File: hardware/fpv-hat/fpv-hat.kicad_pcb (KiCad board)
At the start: 2 copper layers, 100 x 65 mm, 0 parts

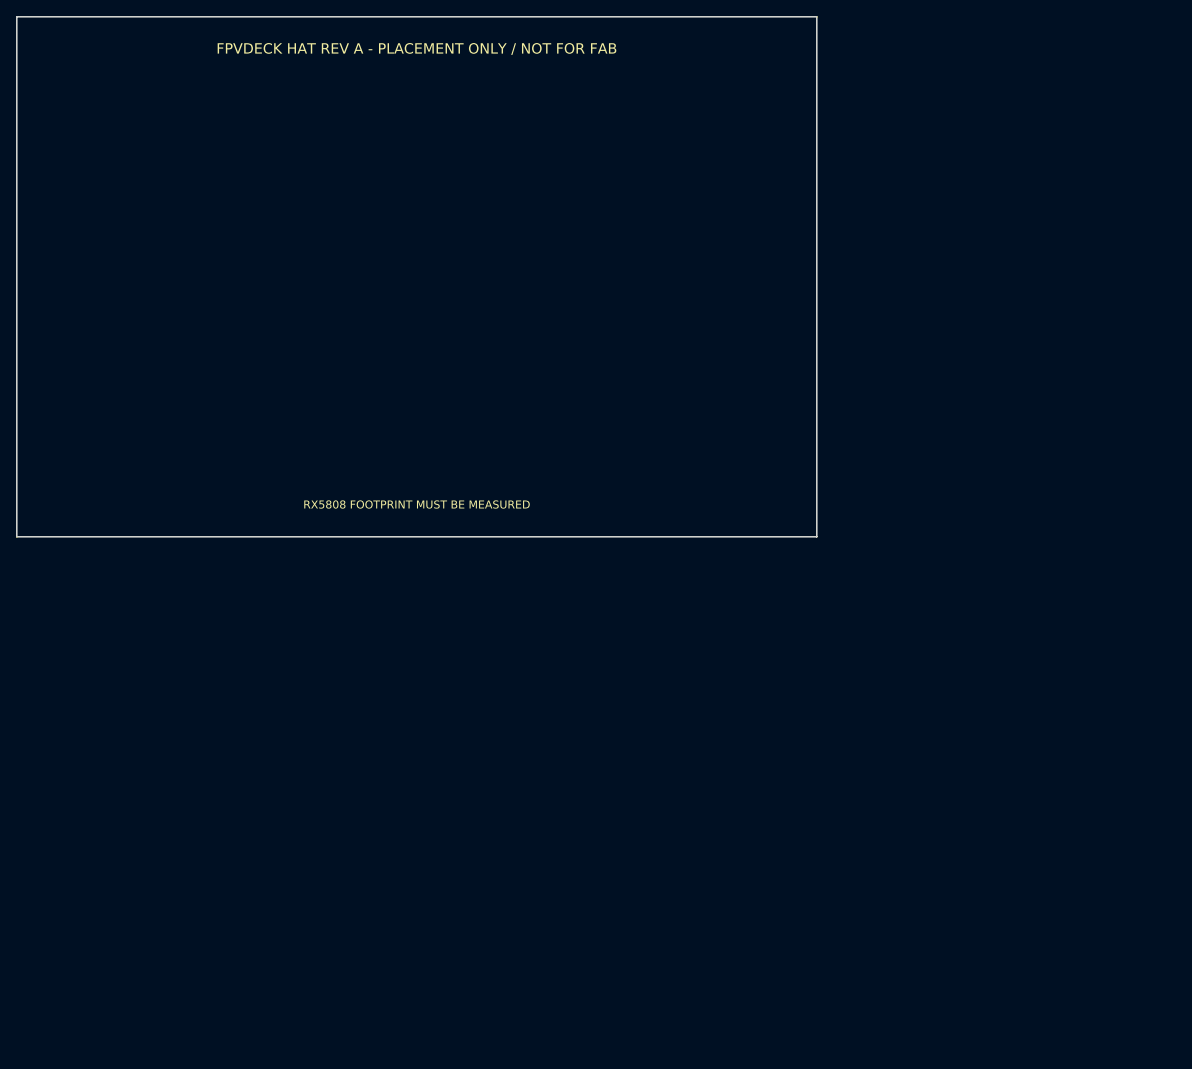
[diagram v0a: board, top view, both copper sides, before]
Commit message: feat(cad): add prototype enclosure and HAT placement model
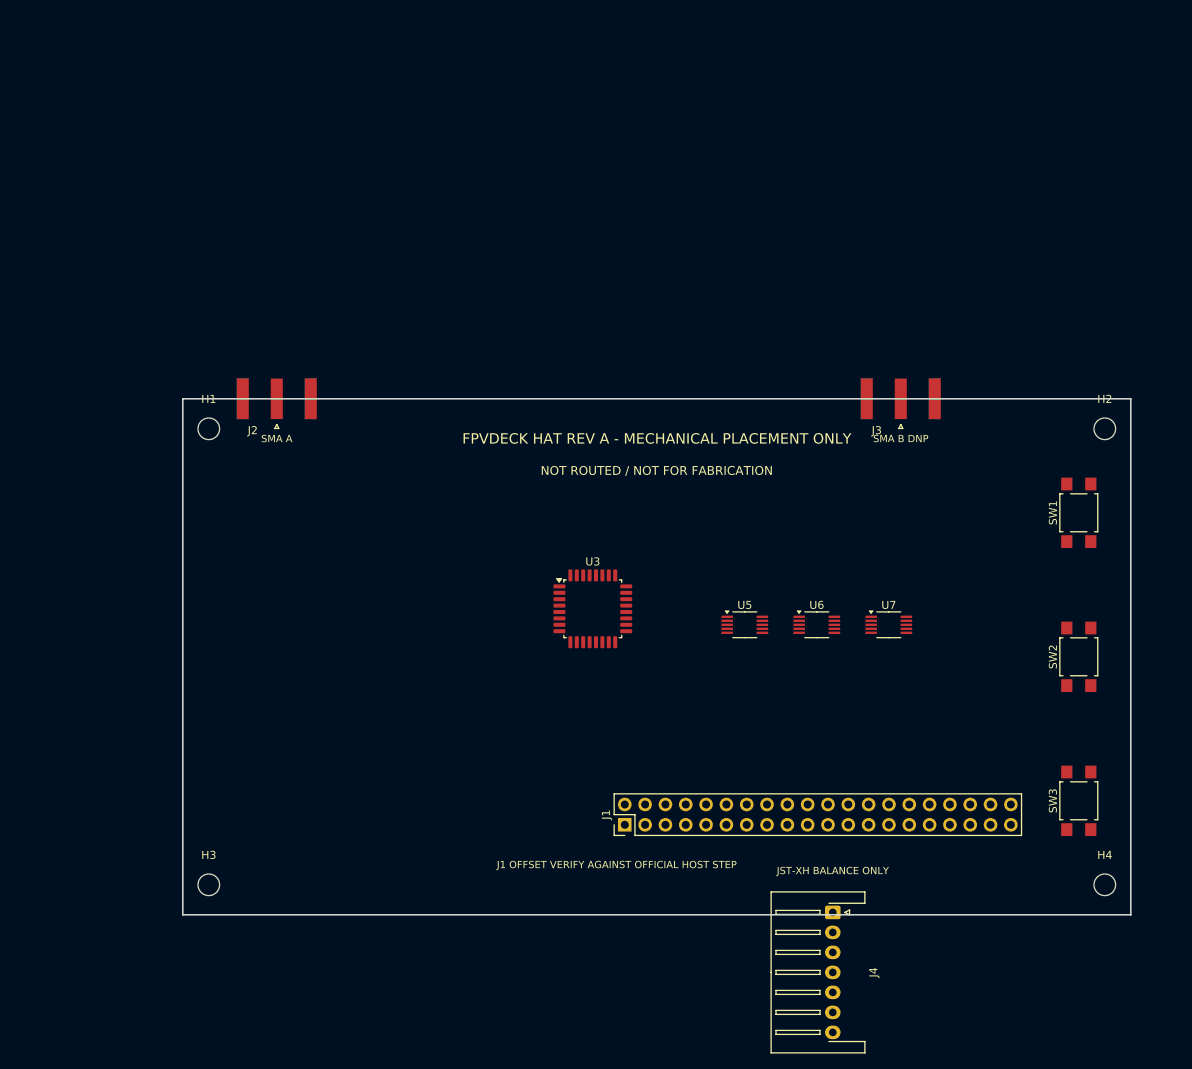
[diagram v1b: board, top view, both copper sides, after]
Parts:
- added H1: MountingHole_2.7mm_M2.5, MountingHole_2.7mm_M2.5, F.Cu at (44.0, 71.5)
- added H2: MountingHole_2.7mm_M2.5, MountingHole_2.7mm_M2.5, F.Cu at (156.0, 71.5)
- added H3: MountingHole_2.7mm_M2.5, MountingHole_2.7mm_M2.5, F.Cu at (44.0, 128.5)
- added H4: MountingHole_2.7mm_M2.5, MountingHole_2.7mm_M2.5, F.Cu at (156.0, 128.5)
- added J1: PinHeader_2x20_P2.54mm_Vertical, PinHeader_2x20_P2.54mm_Vertical, F.Cu at (96.0, 121.0)
- added J2: SMA_Amphenol_132289_EdgeMount, SMA_Amphenol_132289_EdgeMount, F.Cu at (52.5, 67.8)
- added J3: SMA_Amphenol_132289_EdgeMount, SMA_Amphenol_132289_EdgeMount, F.Cu at (130.5, 67.8)
- added J4: JST_XH_S7B-XH-A-1_1x07_P2.50mm_Horizontal, JST_XH_S7B-XH-A-1_1x07_P2.50mm_Horizontal, F.Cu at (122.0, 131.9)
- added SW1: SW_SPST_TL3305A, SW_SPST_TL3305A, F.Cu at (152.8, 82.0)
- added SW2: SW_SPST_TL3305A, SW_SPST_TL3305A, F.Cu at (152.8, 100.0)
- added SW3: SW_SPST_TL3305A, SW_SPST_TL3305A, F.Cu at (152.8, 118.0)
- added U3: LQFP-32_7x7mm_P0.8mm, LQFP-32_7x7mm_P0.8mm, F.Cu at (92.0, 94.0)
- added U5: VSSOP-10_3x3mm_P0.5mm, VSSOP-10_3x3mm_P0.5mm, F.Cu at (111.0, 96.0)
- added U6: VSSOP-10_3x3mm_P0.5mm, VSSOP-10_3x3mm_P0.5mm, F.Cu at (120.0, 96.0)
- added U7: VSSOP-10_3x3mm_P0.5mm, VSSOP-10_3x3mm_P0.5mm, F.Cu at (129.0, 96.0)
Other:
- board size 100 x 65 mm -> 118.5 x 64.5 mm
- board text added: "FPVDECK HAT REV A - MECHANICAL PLACEMENT ONLY"
- board text added: "J1 OFFSET VERIFY AGAINST OFFICIAL HOST STEP"
- board text added: "JST-XH BALANCE ONLY"
- board text added: "NOT ROUTED / NOT FOR FABRICATION"
- board text added: "SMA A"
- board text added: "SMA B DNP"
- board text removed: "FPVDECK HAT REV A - PLACEMENT ONLY / NOT FOR FAB"
- board text removed: "RX5808 FOOTPRINT MUST BE MEASURED"

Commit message: feat(hw): add dual RX5808 final-form HAT layout
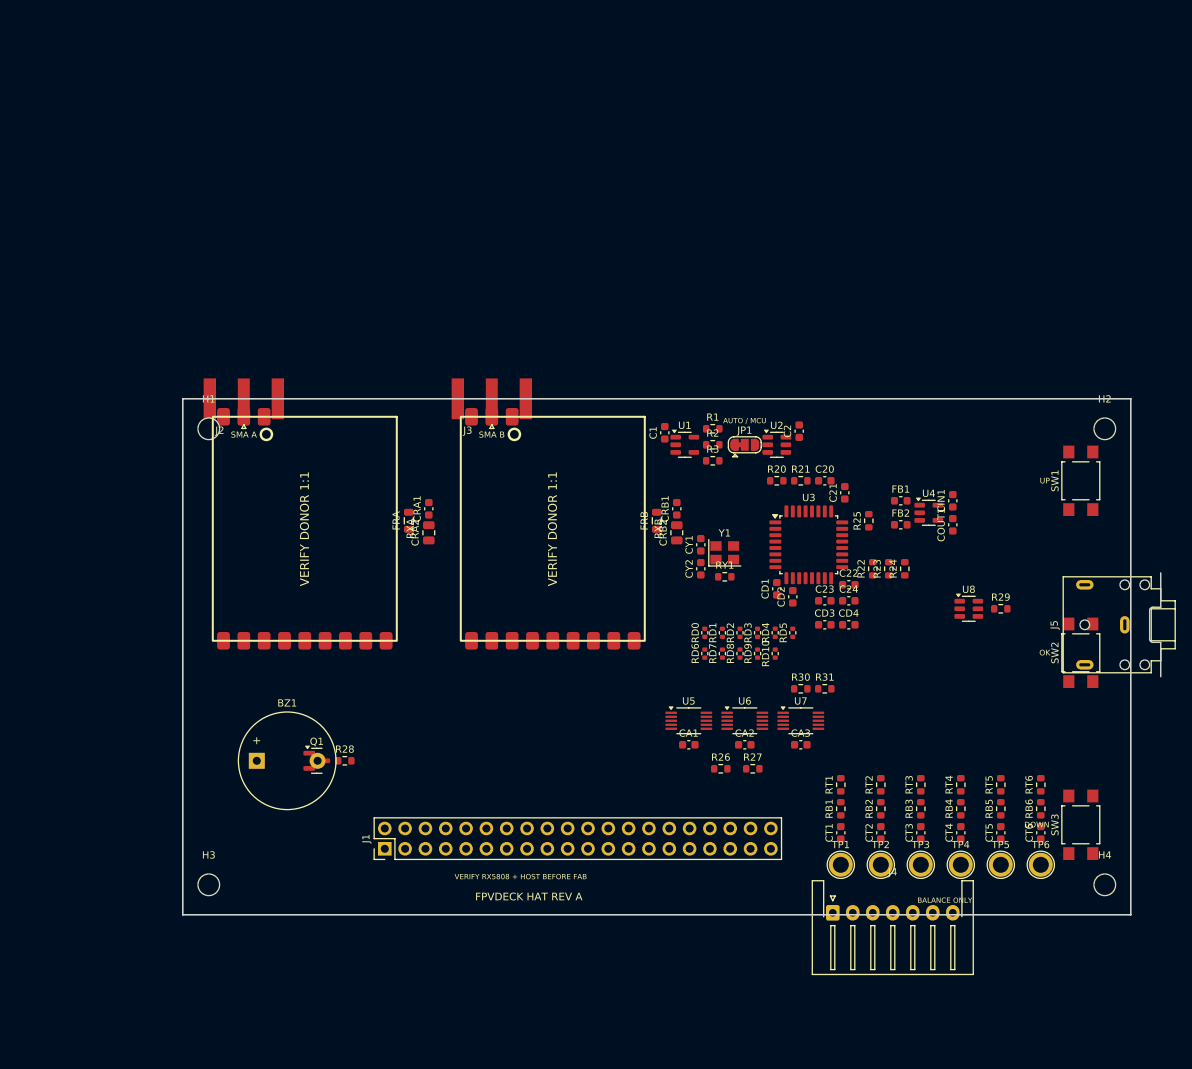
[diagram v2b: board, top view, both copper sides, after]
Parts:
- added BZ1: MAGNETIC BUZZER, Buzzer_12x9.5RM7.6, F.Cu at (50.0, 113.0)
- added C1: 100n 16V X7R, C_0603_1608Metric, F.Cu at (101.0, 72.0)
- added C2: 100n 16V X7R, C_0603_1608Metric, F.Cu at (117.8, 71.8)
- added C20: 100n, C_0603_1608Metric, F.Cu at (121.0, 78.0)
- added C21: 100n, C_0603_1608Metric, F.Cu at (123.5, 79.5)
- added C22: 1u, C_0603_1608Metric, F.Cu at (124.0, 91.0)
- added C23: 1u, C_0603_1608Metric, F.Cu at (121.0, 93.0)
- added C24: 1u, C_0603_1608Metric, F.Cu at (124.0, 93.0)
- added CA1: 100n 16V X7R, C_0603_1608Metric, F.Cu at (104.0, 111.0)
- added CA2: 100n 16V X7R, C_0603_1608Metric, F.Cu at (111.0, 111.0)
- added CA3: 100n 16V X7R, C_0603_1608Metric, F.Cu at (118.0, 111.0)
- added CD1: 100n 16V X7R, C_0603_1608Metric, F.Cu at (115.0, 91.5)
- added CD2: 100n 16V X7R, C_0603_1608Metric, F.Cu at (117.0, 92.5)
- added CD3: 100n 16V X7R, C_0603_1608Metric, F.Cu at (121.0, 96.0)
- added CD4: 100n 16V X7R, C_0603_1608Metric, F.Cu at (124.0, 96.0)
- added CIN1: 1u 10V X7R, C_0603_1608Metric, F.Cu at (137.0, 80.5)
- added COUT1: 1u 10V X7R, C_0603_1608Metric, F.Cu at (137.0, 83.5)
- added CRA1: 100n 16V X7R, C_0603_1608Metric, F.Cu at (71.5, 81.5)
- added CRA2: 10u 10V X7R, C_0805_2012Metric, F.Cu at (71.5, 84.5)
- added CRB1: 100n 16V X7R, C_0603_1608Metric, F.Cu at (102.5, 81.5)
- added CRB2: 10u 10V X7R, C_0805_2012Metric, F.Cu at (102.5, 84.5)
- added CT1: 10n 50V C0G, C_0603_1608Metric, F.Cu at (123.0, 122.0)
- added CT2: 10n 50V C0G, C_0603_1608Metric, F.Cu at (128.0, 122.0)
- added CT3: 10n 50V C0G, C_0603_1608Metric, F.Cu at (133.0, 122.0)
- added CT4: 10n 50V C0G, C_0603_1608Metric, F.Cu at (138.0, 122.0)
- added CT5: 10n 50V C0G, C_0603_1608Metric, F.Cu at (143.0, 122.0)
- added CT6: 10n 50V C0G, C_0603_1608Metric, F.Cu at (148.0, 122.0)
- added CY1: CRYSTAL LOAD TUNE, C_0603_1608Metric, F.Cu at (105.5, 86.0)
- added CY2: CRYSTAL LOAD TUNE, C_0603_1608Metric, F.Cu at (105.5, 89.0)
- added FB1: 600R@100MHz, L_0603_1608Metric, F.Cu at (130.5, 80.5)
- added FB2: 600R@100MHz, L_0603_1608Metric, F.Cu at (130.5, 83.5)
- added FRA: 220R@100MHz 2A, L_0805_2012Metric, F.Cu at (69.0, 83.0)
- added FRB: 220R@100MHz 2A, L_0805_2012Metric, F.Cu at (100.0, 83.0)
- added J5: AV OUT 3.5MM, Jack_3.5mm_CUI_SJ1-3523N_Horizontal, F.Cu at (158.5, 96.0)
- added JP1: AUTO / MCU SELECT, SolderJumper-3_P1.3mm_Bridged12_RoundedPad1.0x1.5mm, F.Cu at (111.0, 73.5)
- added Q1: BUZZER DRIVER, SOT-23, F.Cu at (57.5, 113.0)
- added R1: 10k 1%, R_0603_1608Metric, F.Cu at (107.0, 71.5)
- added R2: 1M 1%, R_0603_1608Metric, F.Cu at (107.0, 73.5)
- added R20: 37.4R 1%, R_0603_1608Metric, F.Cu at (115.0, 78.0)
- added R21: 37.4R 1%, R_0603_1608Metric, F.Cu at (118.0, 78.0)
- added R22: 10k, R_0603_1608Metric, F.Cu at (127.0, 89.0)
- added R23: 10k, R_0603_1608Metric, F.Cu at (129.0, 89.0)
- added R24: 10k, R_0603_1608Metric, F.Cu at (131.0, 89.0)
- added R25: 10k, R_0603_1608Metric, F.Cu at (126.5, 83.0)
- added R26: 100k, R_0603_1608Metric, F.Cu at (108.0, 114.0)
- added R27: 100k, R_0603_1608Metric, F.Cu at (112.0, 114.0)
- added R28: 2.2k, R_0603_1608Metric, F.Cu at (61.0, 113.0)
- added R29: 75R, R_0603_1608Metric, F.Cu at (143.0, 94.0)
- added R3: 10k 1%, R_0603_1608Metric, F.Cu at (107.0, 75.5)
- added R30: 1k, R_0603_1608Metric, F.Cu at (118.0, 104.0)
- added R31: 1k, R_0603_1608Metric, F.Cu at (121.0, 104.0)
- added RB1: 12k 1%, R_0603_1608Metric, F.Cu at (123.0, 119.0)
- added RB2: 12k 1%, R_0603_1608Metric, F.Cu at (128.0, 119.0)
- added RB3: 12k 1%, R_0603_1608Metric, F.Cu at (133.0, 119.0)
- added RB4: 12k 1%, R_0603_1608Metric, F.Cu at (138.0, 119.0)
- added RB5: 12k 1%, R_0603_1608Metric, F.Cu at (143.0, 119.0)
- added RB6: 12k 1%, R_0603_1608Metric, F.Cu at (148.0, 119.0)
- added RD0: 33R 1%, R_0402_1005Metric, F.Cu at (106.0, 97.0)
- added RD1: 33R 1%, R_0402_1005Metric, F.Cu at (108.2, 97.0)
- added RD10: 33R 1%, R_0402_1005Metric, F.Cu at (114.8, 99.6)
- added RD2: 33R 1%, R_0402_1005Metric, F.Cu at (110.4, 97.0)
- added RD3: 33R 1%, R_0402_1005Metric, F.Cu at (112.6, 97.0)
- added RD4: 33R 1%, R_0402_1005Metric, F.Cu at (114.8, 97.0)
- added RD5: 33R 1%, R_0402_1005Metric, F.Cu at (117.0, 97.0)
- added RD6: 33R 1%, R_0402_1005Metric, F.Cu at (106.0, 99.6)
- added RD7: 33R 1%, R_0402_1005Metric, F.Cu at (108.2, 99.6)
- added RD8: 33R 1%, R_0402_1005Metric, F.Cu at (110.4, 99.6)
- added RD9: 33R 1%, R_0402_1005Metric, F.Cu at (112.6, 99.6)
- added RT1: 100k 1%, R_0603_1608Metric, F.Cu at (123.0, 116.0)
- added RT2: 100k 1%, R_0603_1608Metric, F.Cu at (128.0, 116.0)
- added RT3: 100k 1%, R_0603_1608Metric, F.Cu at (133.0, 116.0)
- added RT4: 100k 1%, R_0603_1608Metric, F.Cu at (138.0, 116.0)
- added RT5: 100k 1%, R_0603_1608Metric, F.Cu at (143.0, 116.0)
- added RT6: 100k 1%, R_0603_1608Metric, F.Cu at (148.0, 116.0)
- added RXA: RX5808 MODULE A, RX5808_V1_PROVISIONAL, F.Cu at (56.0, 84.0)
- added RXB: RX5808 MODULE B, RX5808_V1_PROVISIONAL, F.Cu at (87.0, 84.0)
- added RY1: 100k 1%, R_0603_1608Metric, F.Cu at (108.5, 90.0)
- added TP1: TAP1, TestPoint_Plated_Hole_D2.0mm, F.Cu at (123.0, 126.0)
- added TP2: TAP2, TestPoint_Plated_Hole_D2.0mm, F.Cu at (128.0, 126.0)
- added TP3: TAP3, TestPoint_Plated_Hole_D2.0mm, F.Cu at (133.0, 126.0)
- added TP4: TAP4, TestPoint_Plated_Hole_D2.0mm, F.Cu at (138.0, 126.0)
- added TP5: TAP5, TestPoint_Plated_Hole_D2.0mm, F.Cu at (143.0, 126.0)
- added TP6: TAP6, TestPoint_Plated_Hole_D2.0mm, F.Cu at (148.0, 126.0)
- added U1: RSSI COMPARATOR, SOT-23-5, F.Cu at (103.5, 73.5)
- added U2: VIDEO SWITCH, SOT-23-6, F.Cu at (115.0, 73.5)
- added U4: 1.8V LDO, SOT-23-5, F.Cu at (134.0, 82.0)
- added U8: AV BUFFER, SOT-23-6, F.Cu at (139.0, 94.0)
- added Y1: 14.31818MHz, Crystal_SMD_3225-4Pin_3.2x2.5mm, F.Cu at (108.5, 87.0)
- H1, H2, H3, H4: value MountingHole_2.7mm_M2.5 -> M2.5
- J1: value PinHeader_2x20_P2.54mm_Vertical -> WAVESHARE 40PIN
- J2: value SMA_Amphenol_132289_EdgeMount -> SMA EDGE A
- J3: value SMA_Amphenol_132289_EdgeMount -> SMA EDGE B
- J4: value JST_XH_S7B-XH-A-1_1x07_P2.50mm_Horizontal -> BALANCE 2S-6S
- SW1: value SW_SPST_TL3305A -> UP
- SW2: value SW_SPST_TL3305A -> OK
- SW3: value SW_SPST_TL3305A -> DOWN
- U3: value LQFP-32_7x7mm_P0.8mm -> CVBS DECODER
- U5: value VSSOP-10_3x3mm_P0.5mm -> ADS1115 0x48
- U6: value VSSOP-10_3x3mm_P0.5mm -> ADS1115 0x49
- U7: value VSSOP-10_3x3mm_P0.5mm -> ADS1115 0x4A
- moved J3 51.1 mm to (79.4, 67.8)
- moved J1 30.1 mm to (66.0, 124.0)
- moved U3 28.2 mm to (119.0, 86.0)
- moved U7 16.3 mm to (118.0, 108.0)
- moved U6 15.0 mm to (111.0, 108.0)
- moved U5 13.9 mm to (104.0, 108.0)
- moved J2 4.12 mm to (48.4, 67.8)
- moved SW1 4.01 mm to (153.0, 78.0)
- moved SW3 3.01 mm to (153.0, 121.0)
- moved SW2 0.56 mm to (153.0, 99.5)
- moved J4 0.05 mm to (122.0, 132.0), turned to 0 degrees
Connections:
- J1 pad 1: (no net) -> +5V
- J1 pad 11: (no net) -> DVP_D2
- J1 pad 12: (no net) -> DVP_D3
- J1 pad 14: (no net) -> DVP_D4
- J1 pad 15: (no net) -> DVP_D5
- J1 pad 16: (no net) -> DVP_D6
- J1 pad 17: (no net) -> DVP_D7
- J1 pad 18: (no net) -> +3V3
- J1 pad 2: (no net) -> +3V3
- J1 pad 20: (no net) -> DVP_PCLK
- J1 pad 22: (no net) -> DVP_HSYNC
- J1 pad 24: (no net) -> DVP_VSYNC
- J1 pad 26: (no net) -> GND
- J1 pad 28: (no net) -> RX_DATA
- J1 pad 3: (no net) -> +5V
- J1 pad 30: (no net) -> RX_CLK
- J1 pad 31: (no net) -> RX_LE_A
- J1 pad 32: (no net) -> RX_LE_B
- J1 pad 34: (no net) -> VIDEO_SELECT
- J1 pad 35: (no net) -> TVP_RESETB
- J1 pad 36: (no net) -> BTN_UP
- J1 pad 37: (no net) -> BTN_OK
- J1 pad 38: (no net) -> BTN_DOWN
- J1 pad 39: (no net) -> BUZZER
- J1 pad 4: (no net) -> I2C_SDA
- J1 pad 40: (no net) -> GND
- J1 pad 5: (no net) -> GND
- J1 pad 6: (no net) -> I2C_SCL
- J1 pad 7: (no net) -> DVP_D0
- J1 pad 8: (no net) -> VIDEO_SELECT_MCU
- J1 pad 9: (no net) -> DVP_D1
- J2 pad 1: (no net) -> RF_A
- J2 pad 2: (no net) -> GND
- J3 pad 1: (no net) -> RF_B
- J3 pad 2: (no net) -> GND
- J4 pad 1: (no net) -> GND
- J4 pad 2: (no net) -> TAP1
- J4 pad 3: (no net) -> TAP2
- J4 pad 4: (no net) -> TAP3
- J4 pad 5: (no net) -> TAP4
- J4 pad 6: (no net) -> TAP5
- J4 pad 7: (no net) -> TAP6
- SW1 pad 1: (no net) -> BTN_UP
- SW1 pad 2: (no net) -> GND
- SW2 pad 1: (no net) -> BTN_OK
- SW2 pad 2: (no net) -> GND
- SW3 pad 1: (no net) -> BTN_DOWN
- SW3 pad 2: (no net) -> GND
- U3 pad 1: (no net) -> TVP_AIP1A
- U3 pad 10: (no net) -> +3V3
- U3 pad 11: (no net) -> DVP_D7_RAW
- U3 pad 12: (no net) -> DVP_D6_RAW
- U3 pad 13: (no net) -> DVP_D5_RAW
- U3 pad 14: (no net) -> DVP_D4_RAW
- U3 pad 15: (no net) -> DVP_D3_RAW
- U3 pad 16: (no net) -> DVP_D2_RAW
- U3 pad 17: (no net) -> DVP_D1_RAW
- U3 pad 18: (no net) -> DVP_D0_RAW
- U3 pad 19: (no net) -> GND
- U3 pad 2: (no net) -> TVP_AIP1B
- U3 pad 20: (no net) -> +1V8D
- U3 pad 21: (no net) -> I2C_SCL
- U3 pad 22: (no net) -> I2C_SDA
- U3 pad 23: (no net) -> FID_PD
- U3 pad 24: (no net) -> DVP_VSYNC_RAW
- U3 pad 25: (no net) -> DVP_HSYNC_RAW
- U3 pad 26: (no net) -> AVID_PD
- U3 pad 27: (no net) -> INTREQ_PD
- U3 pad 28: (no net) -> +3V3
- U3 pad 29: (no net) -> REFP
- U3 pad 3: (no net) -> AGND
- U3 pad 30: (no net) -> REFM
- U3 pad 31: (no net) -> AGND
- U3 pad 32: (no net) -> +1V8A
- U3 pad 4: (no net) -> +1V8A
- U3 pad 5: (no net) -> XTAL1
- U3 pad 6: (no net) -> XTAL2
- U3 pad 7: (no net) -> AGND
- U3 pad 8: (no net) -> TVP_RESETB
- U3 pad 9: (no net) -> DVP_PCLK_RAW
- U5 pad 1: (no net) -> GND
- U5 pad 10: (no net) -> I2C_SCL
- U5 pad 2: (no net) -> ADC1_ALERT
- U5 pad 3: (no net) -> GND
- U5 pad 4: (no net) -> TAP1_ADC
- U5 pad 5: (no net) -> TAP2_ADC
- U5 pad 6: (no net) -> TAP3_ADC
- U5 pad 7: (no net) -> TAP4_ADC
- U5 pad 8: (no net) -> +3V3
- U5 pad 9: (no net) -> I2C_SDA
- U6 pad 1: (no net) -> +3V3
- U6 pad 10: (no net) -> I2C_SCL
- U6 pad 2: (no net) -> ADC2_ALERT
- U6 pad 3: (no net) -> GND
- U6 pad 4: (no net) -> TAP5_ADC
- U6 pad 5: (no net) -> TAP6_ADC
- U6 pad 6: (no net) -> DECK_ADC
- U6 pad 7: (no net) -> SPARE_ADC
- U6 pad 8: (no net) -> +3V3
- U6 pad 9: (no net) -> I2C_SDA
- U7 pad 1: (no net) -> I2C_SDA
- U7 pad 10: (no net) -> I2C_SCL
- U7 pad 2: (no net) -> ADC3_ALERT
- U7 pad 3: (no net) -> GND
- U7 pad 4: (no net) -> RSSI_A_ADC
- U7 pad 5: (no net) -> RSSI_B_ADC
- U7 pad 6: (no net) -> SPARE_RSSI2
- U7 pad 7: (no net) -> SPARE_RSSI3
- U7 pad 8: (no net) -> +3V3
- U7 pad 9: (no net) -> I2C_SDA
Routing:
- net RF_B: track 0.00 -> 2.25 mm
- net RF_A: track 0.00 -> 2.25 mm
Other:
- copper layers 2 -> 4
- board text added: "AUTO / MCU"
- board text added: "BALANCE ADC"
- board text added: "BALANCE ONLY"
- board text added: "DOWN"
- board text added: "FPVDECK HAT REV A"
- board text added: "OK"
- board text added: "RX A"
- board text added: "RX B"
- board text added: "SMA B"
- board text added: "UP"
- board text added: "VERIFY RX5808 + HOST BEFORE FAB"
- board text added: "VIDEO / DIVERSITY"
- board text removed: "FPVDECK HAT REV A - MECHANICAL PLACEMENT ONLY"
- board text removed: "J1 OFFSET VERIFY AGAINST OFFICIAL HOST STEP"
- board text removed: "JST-XH BALANCE ONLY"
- board text removed: "NOT ROUTED / NOT FOR FABRICATION"
- board text removed: "SMA B DNP"

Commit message: fix(hw): correct LMV331 diversity pin mapping
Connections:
- U1 pad 1: RX_A_STRONGER -> RSSI_A_HYS
- U1 pad 3: RSSI_A_HYS -> RSSI_B
- U1 pad 4: RSSI_B -> RX_A_STRONGER

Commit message: fix(hw): complete verified buffered AV output
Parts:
- added C25: 100n 16V X7R, C_0603_1608Metric, F.Cu at (136.0, 94.0)
- added C26: 100n 16V X7R, C_0603_1608Metric, F.Cu at (139.0, 90.5)
- added C27: 4.7u 10V X7R, C_0805_2012Metric, F.Cu at (142.0, 90.5)
- R29: value 75R -> 75R 1%
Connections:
- net AV_BUF_BIAS renamed NC_AV3
- U8 pad 1: AV_BUF_IN -> NC_AV1
- U8 pad 2: GND -> AV_BUF_OUT
- U8 pad 4: AV_BUF_EN -> AV_BUF_IN
- U8 pad 5: +5V -> GND
- U8 pad 6: AV_BUF_OUT -> +5V

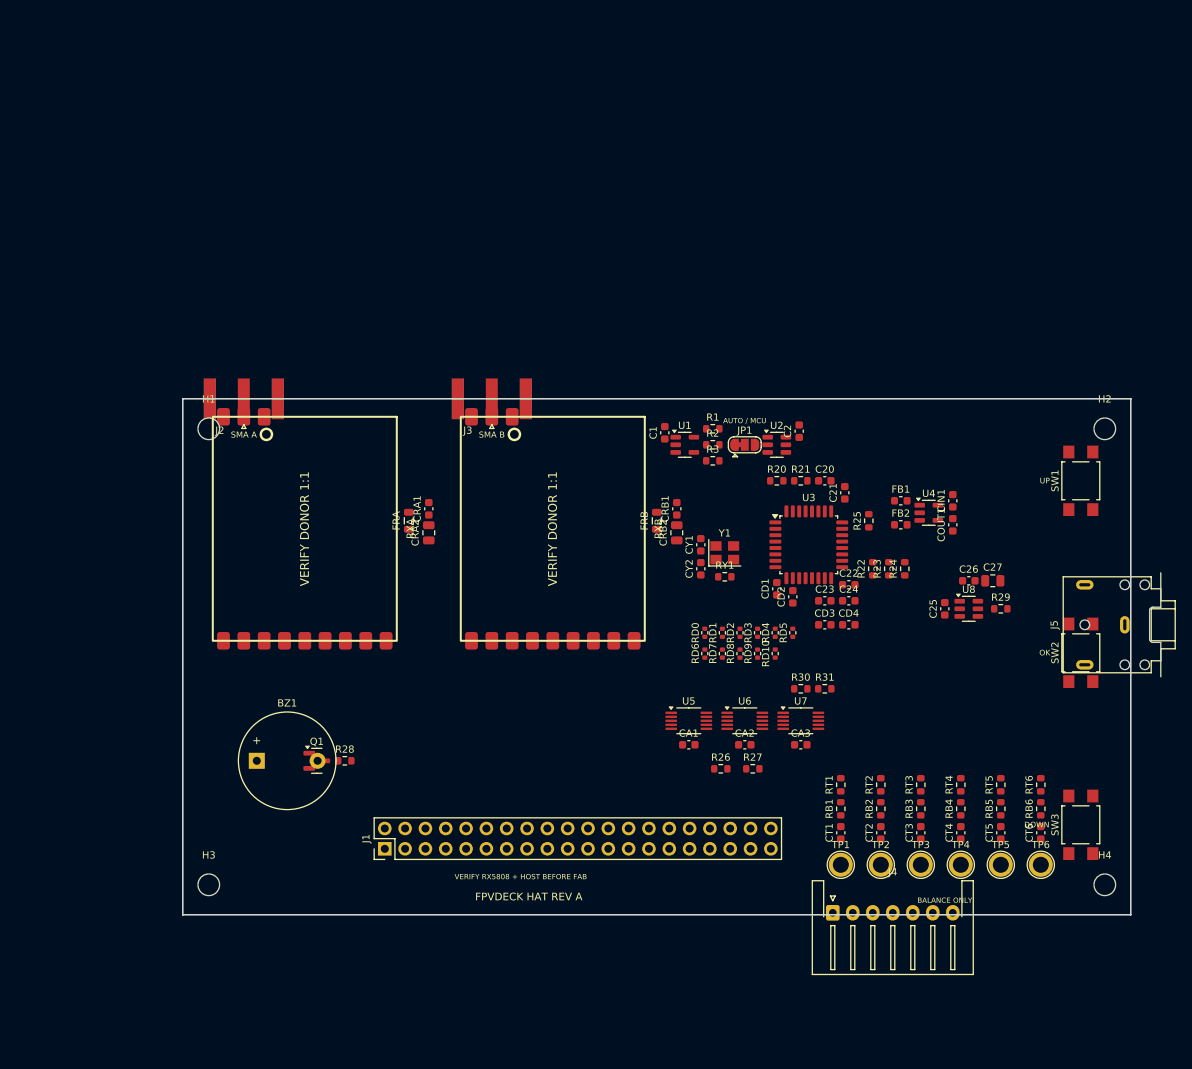
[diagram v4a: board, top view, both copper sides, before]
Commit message: feat(hw): move antennas to left and top-right edges
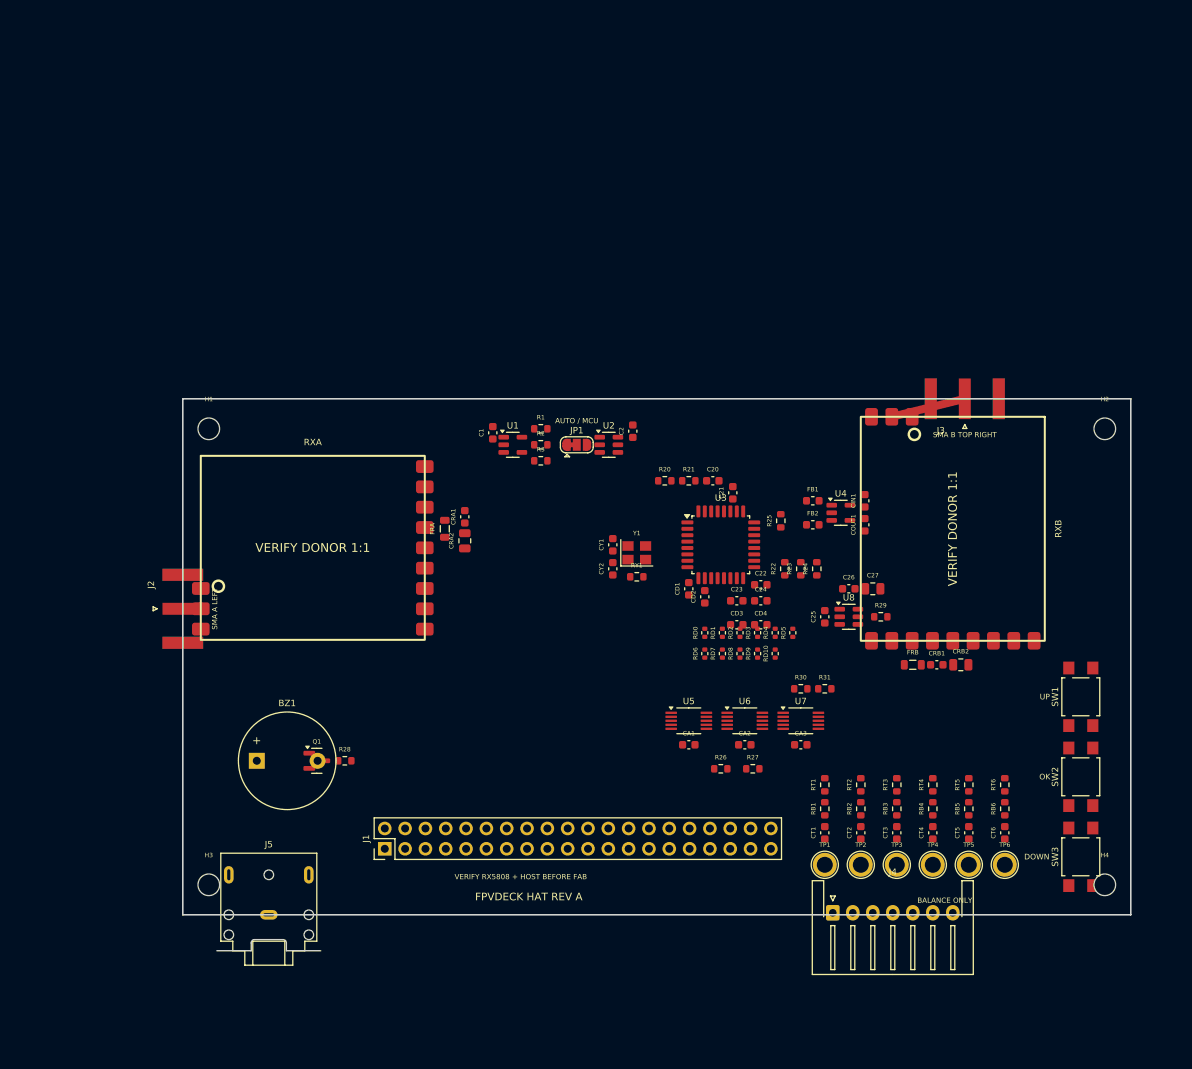
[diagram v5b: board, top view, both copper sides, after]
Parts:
- moved J5 113.0 mm to (51.5, 132.2), turned to 0 degrees
- moved J3 59.1 mm to (138.5, 67.8)
- moved RXB 50.0 mm to (137.0, 84.0)
- moved CRB2 39.1 mm to (138.0, 101.0), turned to 0 degrees
- moved CRB1 37.9 mm to (135.0, 101.0), turned to 0 degrees
- moved FRB 36.7 mm to (132.0, 101.0), turned to 0 degrees
- moved J2 27.3 mm to (40.8, 94.0), turned to 0 degrees
- moved SW1 27.0 mm to (153.0, 105.0)
- moved C1 21.5 mm to (79.5, 72.0)
- moved R1 21.5 mm to (85.5, 71.5)
- moved R2 21.5 mm to (85.5, 73.5)
- moved R3 21.5 mm to (85.5, 75.5)
- moved U1 21.5 mm to (82.0, 73.5)
- moved JP1 21.0 mm to (90.0, 73.5)
- moved U2 21.0 mm to (94.0, 73.5)
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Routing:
- net RF_B: track 2.25 -> 9.39 mm
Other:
- board text added: "RX A / LEFT"
- board text added: "RX B / TOP RIGHT"
- board text added: "SMA A LEFT"
- board text added: "SMA B TOP RIGHT"
- board text removed: "RX A"
- board text removed: "RX B"
- board text removed: "SMA A"
- board text removed: "SMA B"
